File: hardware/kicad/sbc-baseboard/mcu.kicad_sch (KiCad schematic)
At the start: 36 parts, among them J16 SWD, J3 USB-C HID to target, SW201 RESET, U201 MK64FN1M0VLL12, U202 USBLC6-2SC6, Y201 32.768kHz

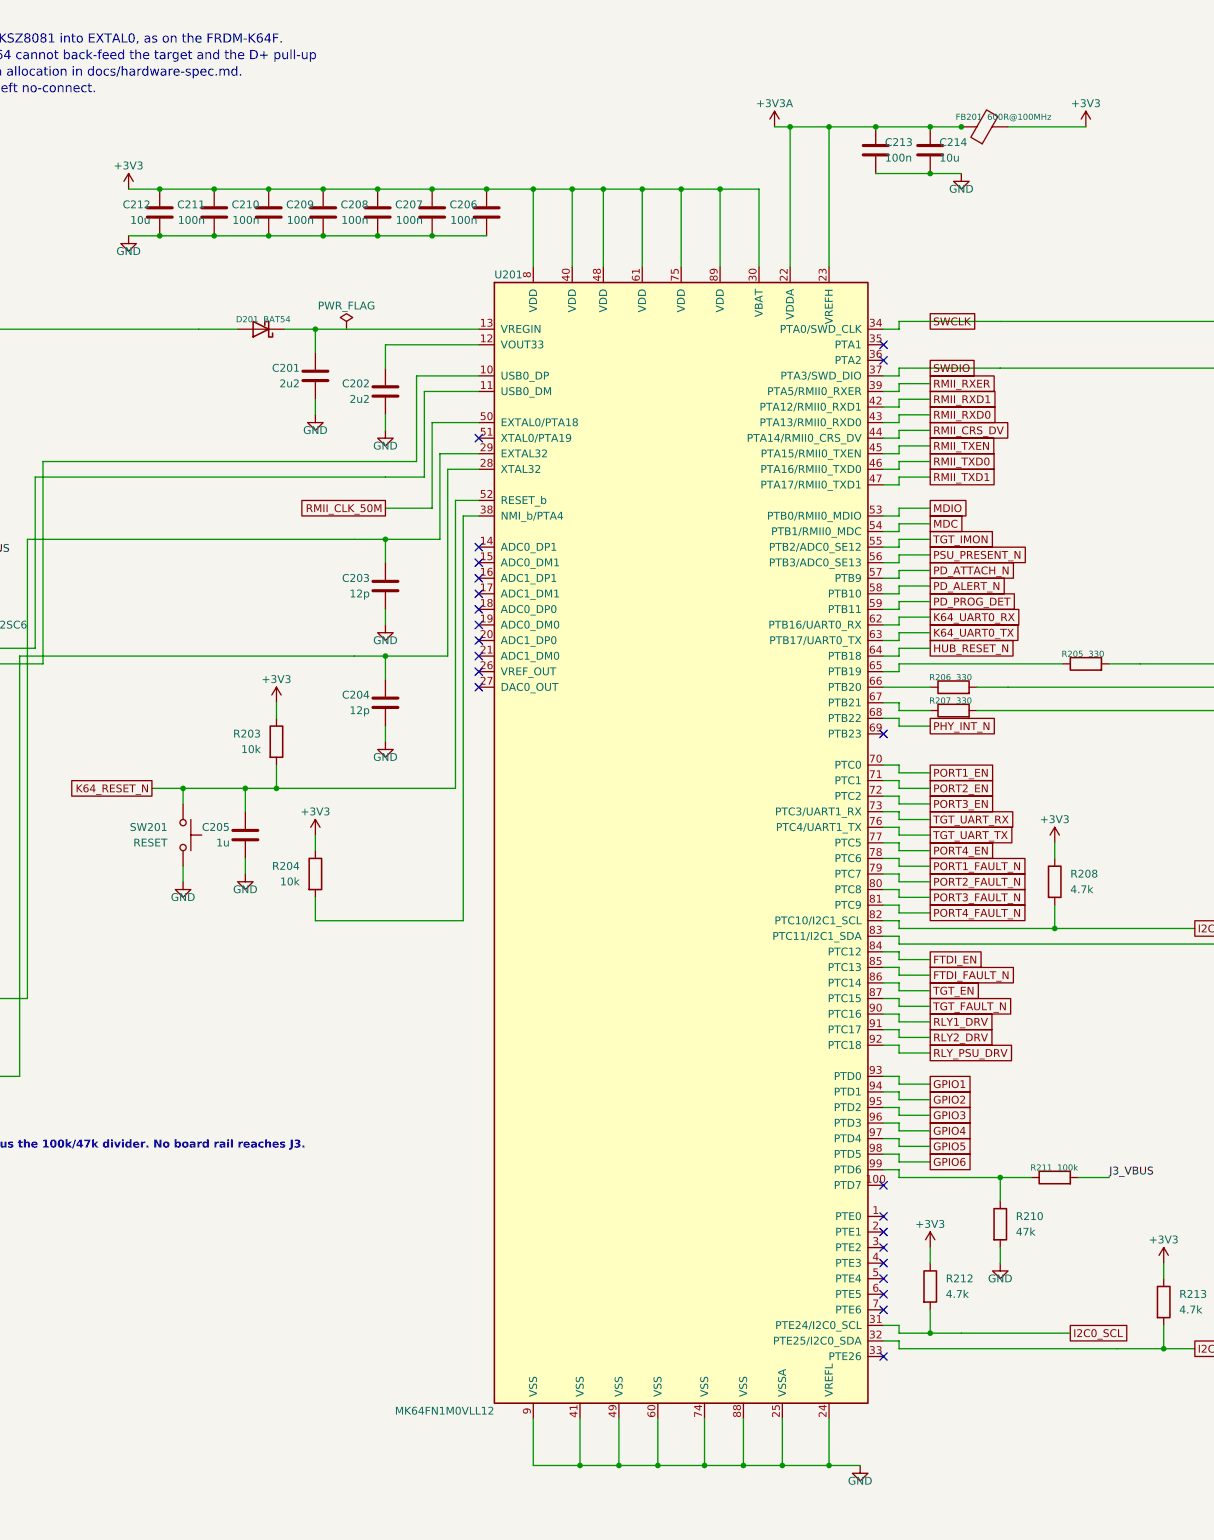
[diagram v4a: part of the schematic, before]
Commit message: Pin-name overlap gate; symbol clearance from shared glyph widths
gen/check_pins.py estimates the box of every visible pin name inside every
symbol on a sheet (KiCad stroke font, per-glyph advance; hidden and stacked
same-name pins skipped) and reports names that print over each other. Run
on the last commit's sheets it finds exactly the overlaps seen on paper
(U402 VDD33/VDDA33 over the first side rows, K64 VDD/VDDA/VREFH/VREFL over
VREGIN, PTA0/SWD_CLK and PTE26, PCA9517A VCC(A)/VCC(B) marginal) and none in
the KiCad library symbols. check_layout.py reports it as the pin-name
category, and --gaps lists the closest name pairs.

parts.py now uses the same glyph widths for the box-symbol clearance, with a
0.8 mm gap: the K64 gets three clearance rows top and bottom (VREFL vs PTE26
was 0.13 mm by this metric). All sheets: pin-name 0, ERC 0, contacts 0,
merges 0, frame 0; connectivity unchanged.

Co-Authored-By: Claude Fable 5.1 <noreply@anthropic.com>
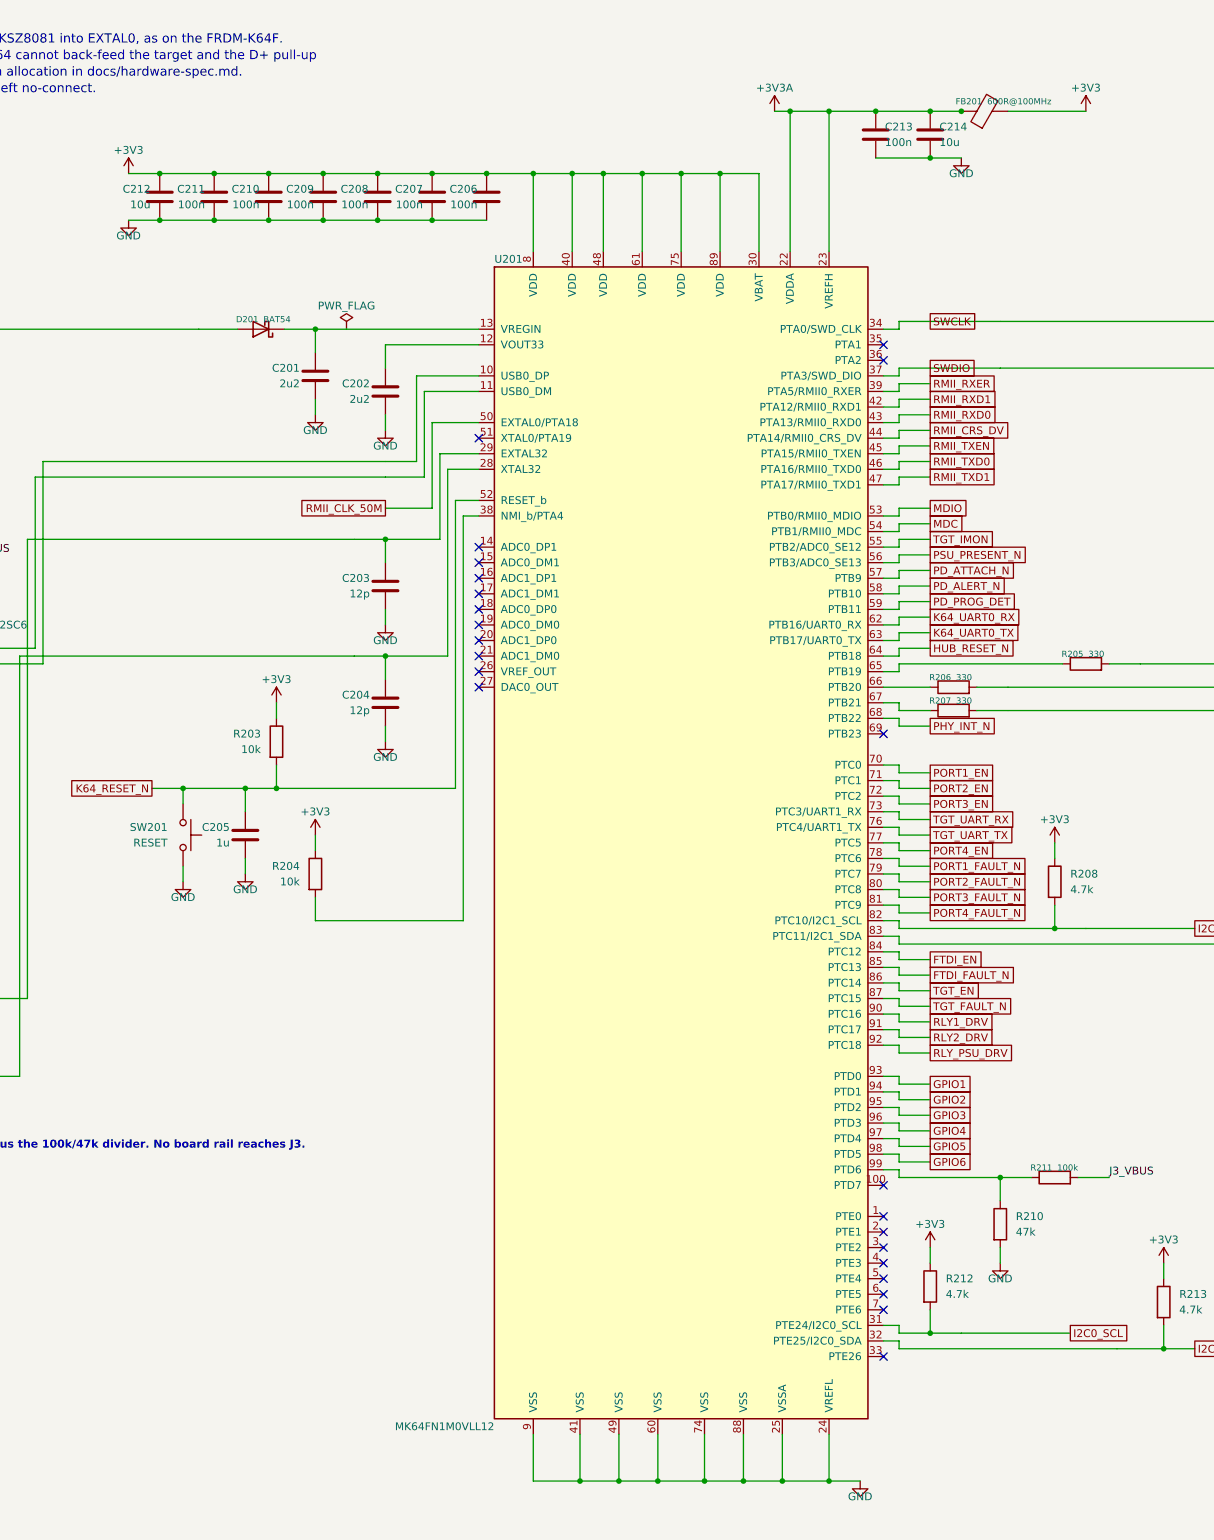
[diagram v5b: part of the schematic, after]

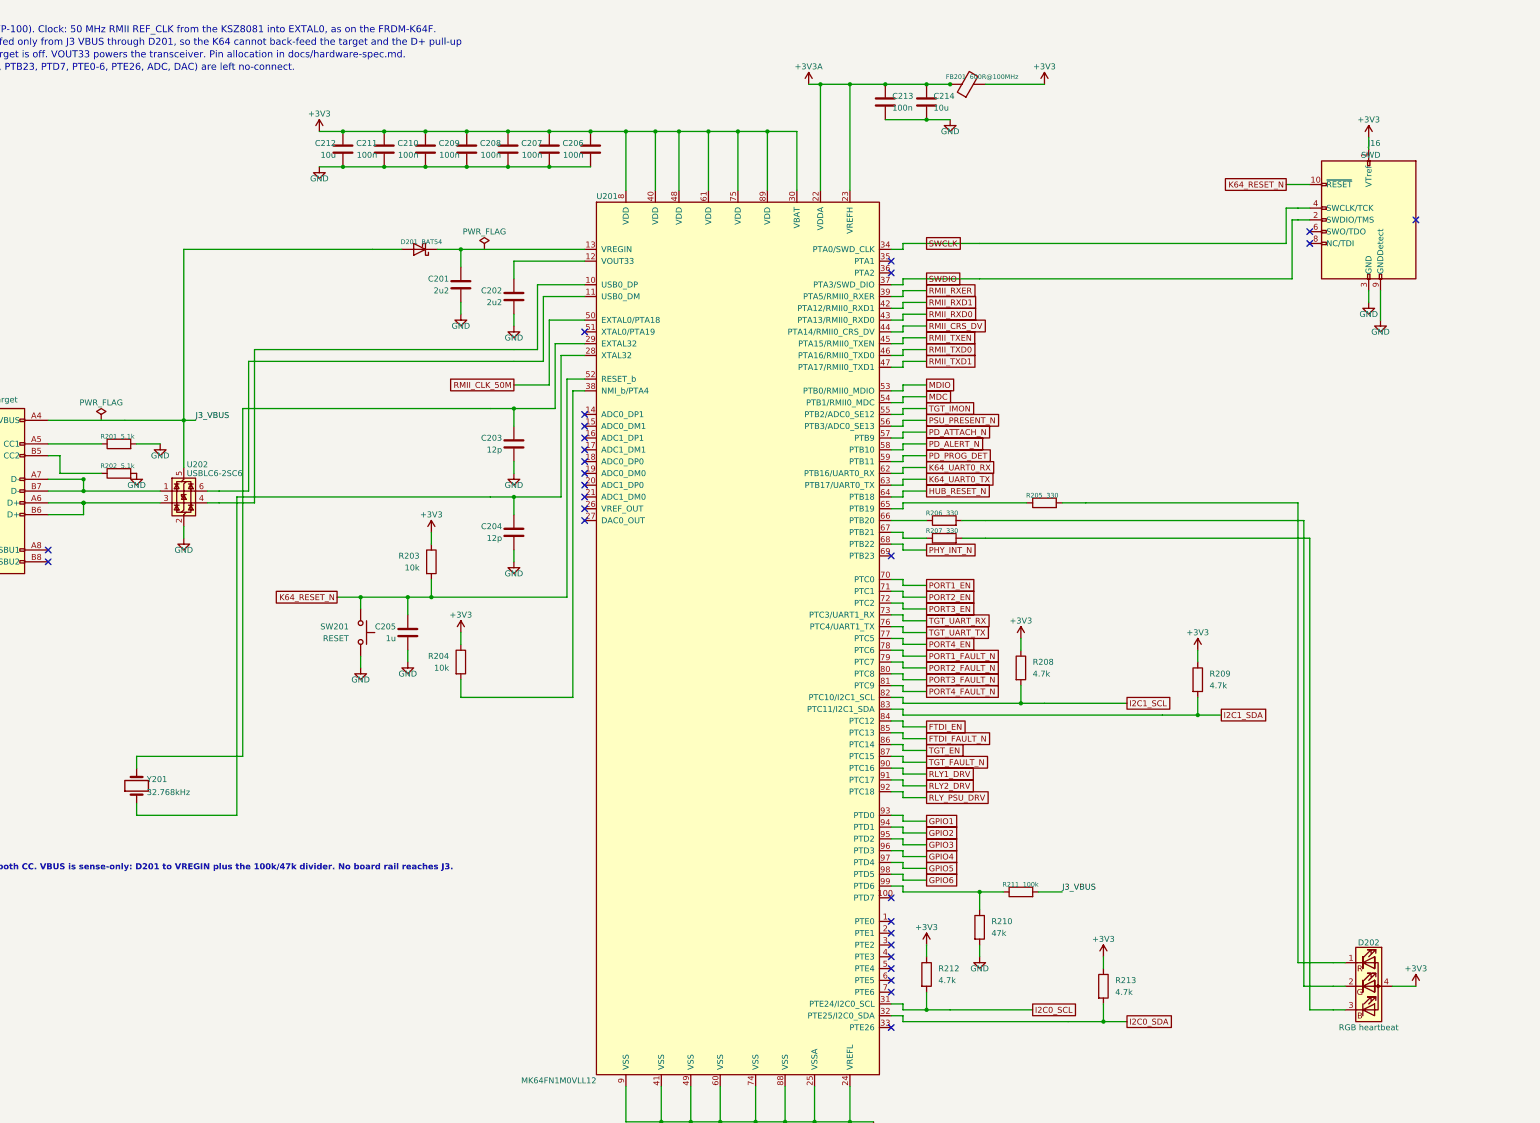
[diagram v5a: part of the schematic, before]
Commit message: Reference-design review; pin numbers and real text widths in the layout gate
Review (docs/reference-design-review.md): every IC's surrounding parts
compared with its datasheet typical application or evaluation board.
Brought in line:
- TPS54560B compensation 16.9k / 4.7 nF / 47 pF (the 5 V / 400 kHz design
  example, same 141 uF ceramic output); the placeholders are gone.
- TPS62823 divider 453k / 100k with the 120 pF feed-forward capacitor the
  datasheet recommends.
- USB2517 VBUS_DET from the EVB: 100k / 100k with 1 uF (was 10k / 22k, 3.4 V
  at a 3.3 V pin).
- KSZ8081 MDIO pull-up 1.0k as the datasheet requires (was 4.7k).
- FT231X: 27 R in series and 47 pF on USBDM/USBDP, datasheet figure 6.1.
Deviations kept and documented: the bucks' EN gated by the PD controller
instead of a UVLO divider, the FT231X fed by a power switch instead of a
ferrite bead, translator OE tied to the target rail.

Layout gate: pin numbers are text boxes like any other, and all text widths
come from a per-glyph table fitted to the extents KiCad writes into its PDF
(check_pins.py); the generator's spacing uses the same table. That exposed
and fixed: reference/value overlaps on narrow symbols (now stacked), rail
names printed over each other (the lane end and hanging pull-up now carry
half the rail name), a port-switch value over its pin number, turned parts
with text on the pin side, lane stacks whose spread collapsed at the grid
snap, routes landing on connector pin stubs (J16, J601, J14, D202 moved),
the PD controller's I2C and gate routes that crossed half the sheet (now
labels), and the port /FAULT and I2C1 pull-ups, which as hanging resistors
staggered off the sheet and are now one column to one +3V3 symbol. The
port switch carries FAULT above OUT so the switched rail's parts hang below
the label; the VBUS row is drawn from the connector back to the switch.

All sheets: ERC 0, contacts 0, merges 0, layout 0 in every category.
Connectivity against 8579cd2 differs only in the value ch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
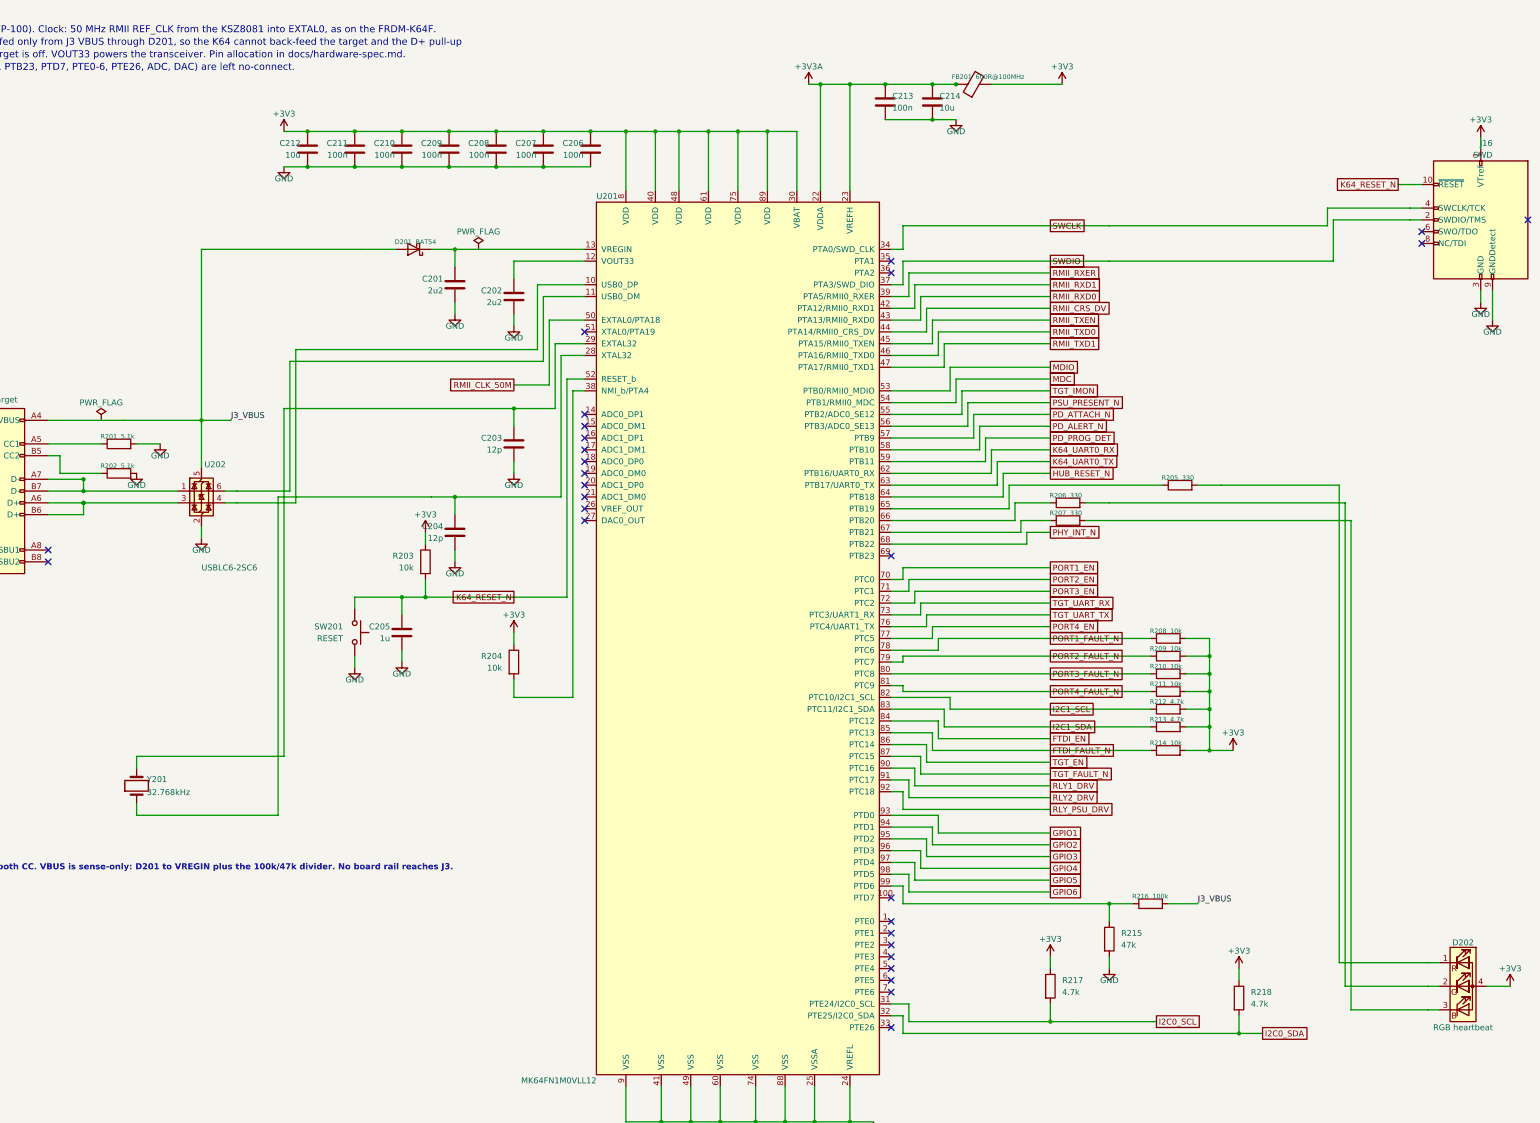
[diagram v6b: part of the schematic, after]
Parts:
- added R214: 10k, Resistor_SMD:R_0603_1608Metric, symbol Device:R
- added R215: 47k, Resistor_SMD:R_0603_1608Metric, symbol Device:R
- added R216: 100k, Resistor_SMD:R_0603_1608Metric, symbol Device:R
- added R217, R218: 4.7k, Resistor_SMD:R_0603_1608Metric, symbol Device:R
- R208, R209: value 4.7k -> 10k
- R210: value 47k -> 10k
- R211: value 100k -> 10k
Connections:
- net +3V3: now also R208.2, R209.2, R210.2, R211.2, R212.2, R213.2, R214.2, R217.1, R218.1; no longer R208.1, R209.1, R212.1, R213.1
- net FTDI_FAULT_N: now also R214.1
- net GND: now also R215.2; no longer R210.2
- net I2C0_SCL: now also R217.2; no longer R212.2
- net I2C0_SDA: now also R218.2; no longer R213.2
- net I2C1_SCL: now also R212.1; no longer R208.2
- net I2C1_SDA: now also R213.1; no longer R209.2
- net J3_VBUS: now also R216.2; no longer R211.2
- net PORT1_FAULT_N: now also R208.1
- net PORT2_FAULT_N: now also R209.1
- net PORT3_FAULT_N: now also R210.1
- net PORT4_FAULT_N: now also R211.1
- new net: R215.1, R216.1, U201.99 (PTD6)
